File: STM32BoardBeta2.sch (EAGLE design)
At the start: 64 parts, among them IC2 LM2576S, IC3 LM1117IDTX-3.3, IC4 FT232RL, J1 DCJ0202, Q1 8MHz, Q2 32.768KHz, SW1 BOOT, U1 STM32F410R3, X1 MINI-USB-32005-201

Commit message: Cambios en condensador y diodo
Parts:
- C3: device rcl:CPOL-EUE7.5-18 -> rcl:CPOL-EUE5-10.5
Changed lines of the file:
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@@
 <grid distance="0.1" unitdist="inch" unit="inch" style="lines" multiple="1" display="no" altdistance="0.01" altunitdist="inch" altunit="inch"/>
 <layers>
-<layer number="1" name="Top" color="4" fill="1" visible="no" active="no"/>
-<layer number="2" name="Route2" color="1" fill="3" visible="no" active="no"/>
-<layer number="3" name="Route3" color="4" fill="3" visible="no" active="no"/>
-<layer number="4" name="Route4" color="1" fill="4" visible="no" active="no"/>
-<layer number="5" name="Route5" color="4" fill="4" visible="no" active="no"/>
-<layer number="6" name="Route6" color="1" fill="8" visible="no" active="no"/>
-<layer number="7" name="Route7" color="4" fill="8" visible="no" active="no"/>
-<layer number="8" name="Route8" color="1" fill="2" visible="no" active="no"/>
-<layer number="9" name="Route9" color="4" fill="2" visible="no" active="no"/>
-<layer number="10" name="Route10" color="1" fill="7" visible="no" active="no"/>
-<layer number="11" name="Route11" color="4" fill="7" visible="no" active="no"/>
-<layer number="12" name="Route12" color="1" fill="5" visible="no" active="no"/>
-<layer number="13" name="Route13" color="4" fill="5" visible="no" active="no"/>
-<layer number="14" name="Route14" color="1" fill="6" visible="no" active="no"/>
-<layer number="15" name="Route15" color="4" fill="6" visible="no" active="no"/>
-<layer number="16" name="Bottom" color="1" fill="1" visible="no" active="no"/>
-<layer number="17" name="Pads" color="2" fill="1" visible="no" active="no"/>
-<layer number="18" name="Vias" color="2" fill="1" visible="no" active="no"/>
-<layer number="19" name="Unrouted" color="6" fill="1" visible="no" active="no"/>
-<layer number="20" name="Dimension" color="15" fill="1" visible="no" active="no"/>
-<layer number="21" name="tPlace" color="7" fill="1" visible="no" active="no"/>
-<layer number="22" name="bPlace" color="7" fill="1" visible="no" active="no"/>
-<layer number="23" name="tOrigins" color="15" fill="1" visible="no" active="no"/>
-<layer number="24" name="bOrigins" color="15" fill="1" visible="no" active="no"/>
-<layer number="25" name="tNames" color="7" fill="1" visible="no" active="no"/>
-<layer number="26" name="bNames" color="7" fill="1" visible="no" active="no"/>
-<layer number="27" name="tValues" color="7" fill="1" visible="no" active="no"/>
-<layer number="28" name="bValues" color="7" fill="1" visible="no" active="no"/>
+<layer number="1" name="Top" color="4" fill="1" visible="yes" active="no"/>
+<layer number="2" name="Route2" color="1" fill="3" visible="yes" active="no"/>
+<layer number="3" name="Route3" color="4" fill="3" visible="yes" active="no"/>
+<layer number="4" name="Route4" color="1" fill="4" visible="yes" active="no"/>
+<layer number="5" name="Route5" color="4" fill="4" visible="yes" active="no"/>
+<layer number="6" name="Route6" color="1" fill="8" visible="yes" active="no"/>
+<layer number="7" name="Route7" color="4" fill="8" visible="yes" active="no"/>
+<layer number="8" name="Route8" color="1" fill="2" visible="yes" active="no"/>
+<layer number="9" name="Route9" color="4" fill="2" visible="yes" active="no"/>
+<layer number="10" name="Route10" color="1" fill="7" visible="yes" active="no"/>
+<layer number="11" name="Route11" color="4" fill="7" visible="yes" active="no"/>
+<layer number="12" name="Route12" color="1" fill="5" visible="yes" active="no"/>
+<layer number="13" name="Route13" color="4" fill="5" visible="yes" active="no"/>
+<layer number="14" name="Route14" color="1" fill="6" visible="yes" active="no"/>
+<layer number="15" name="Route15" color="4" fill="6" visible="yes" active="no"/>
+<layer number="16" name="Bottom" color="1" fill="1" visible="yes" active="no"/>
+<layer number="17" name="Pads" color="2" fill="1" visible="yes" active="no"/>
+<layer number="18" name="Vias" color="2" fill="1" visible="yes" active="no"/>
+<layer number="19" name="Unrouted" color="6" fill="1" visible="yes" active="no"/>
+<layer number="20" name="Dimension" color="15" fill="1" visible="yes" active="no"/>
+<layer number="21" name="tPlace" color="7" fill="1" visible="yes" active="no"/>
+<layer number="22" name="bPlace" color="7" fill="1" visible="yes" active="no"/>
+<layer number="23" name="tOrigins" color="15" fill="1" visible="yes" active="no"/>
+<layer number="24" name="bOrigins" color="15" fill="1" visible="yes" active="no"/>
+<layer number="25" name="tNames" color="7" fill="1" visible="yes" active="no"/>
+<layer number="26" name="bNames" color="7" fill="1" visible="yes" active="no"/>
+<layer number="27" name="tValues" color="7" fill="1" visible="yes" active="no"/>
+<layer number="28" name="bValues" color="7" fill="1" visible="yes" active="no"/>
 <layer number="29" name="tStop" color="7" fill="3" visible="no" active="no"/>
 <layer number="30" name="bStop" color="7" fill="6" visible="no" active="no"/>
@@
 <layer number="35" name="tGlue" color="7" fill="4" visible="no" active="no"/>
 <layer number="36" name="bGlue" color="7" fill="5" visible="no" active="no"/>
-<layer number="37" name="tTest" color="7" fill="1" visible="no" active="no"/>
-<layer number="38" name="bTest" color="7" fill="1" visible="no" active="no"/>
+<layer number="37" name="tTest" color="7" fill="1" visible="yes" active="no"/>
+<layer number="38" name="bTest" color="7" fill="1" visible="yes" active="no"/>
 <layer number="39" name="tKeepout" color="4" fill="11" visible="no" active="no"/>
 <layer number="40" name="bKeepout" color="1" fill="11" visible="no" active="no"/>
@@
 <layer number="44" name="Drills" color="7" fill="1" visible="no" active="no"/>
 <layer number="45" name="Holes" color="7" fill="1" visible="no" active="no"/>
-<layer number="46" name="Milling" color="3" fill="1" visible="no" active="no"/>
-<layer number="47" name="Measures" color="7" fill="1" visible="no" active="no"/>
-<layer number="48" name="Document" color="7" fill="1" visible="no" active="no"/>
-<layer number="49" name="Reference" color="7" fill="1" visible="no" active="no"/>
-<layer number="50" name="dxf" color="7" fill="1" visible="no" active="no"/>
-<layer number="51" name="tDocu" color="7" fill="1" visible="no" active="no"/>
-<layer number="52" name="bDocu" color="7" fill="1" visible="no" active="no"/>
-<layer number="53" name="tGND_GNDA" color="7" fill="1" visible="no" active="no"/>
-<layer number="54" name="bGND_GNDA" color="7" fill="1" visible="no" active="no"/>
-<layer number="56" name="wert" color="7" fill="1" visible="no" active="no"/>
+<layer number="46" name="Milling" color="3" fill="1" visible="yes" active="no"/>
+<layer number="47" name="Measures" color="7" fill="1" visible="yes" active="no"/>
+<layer number="48" name="Document" color="7" fill="1" visible="yes" active="no"/>
+<layer number="49" name="Reference" color="7" fill="1" visible="yes" active="no"/>
+<layer number="50" name="dxf" color="7" fill="1" visible="yes" active="no"/>
+<layer number="51" name="tDocu" color="7" fill="1" visible="yes" active="no"/>
+<layer number="52" name="bDocu" color="7" fill="1" visible="yes" active="no"/>
+<layer number="53" name="tGND_GNDA" color="7" fill="1" visible="yes" active="no"/>
+<layer number="54" name="bGND_GNDA" color="7" fill="1" visible="yes" active="no"/>
+<layer number="56" name="wert" color="7" fill="1" visible="yes" active="no"/>
 <layer number="90" name="Modules" color="5" fill="1" visible="yes" active="yes"/>
 <layer number="91" name="Nets" color="2" fill="1" visible="yes" active="yes"/>
@@
 <part name="GND3" library="supply1" deviceset="GND" device=""/>
 <part name="D2" library="diode" deviceset="1N4004" device="" value="1N5822"/>
-<part name="C3" library="rcl" deviceset="CPOL-EU" device="E7.5-18" value="1000uF"/>
+<part name="C3" library="rcl" deviceset="CPOL-EU" device="E5-10.5" value="1000uF"/>
 <part name="GND4" library="supply1" deviceset="GND" device=""/>
 <part name="IC3" library="lm1117" deviceset="LM1117IDTX-*" device="" technology="3.3"/>

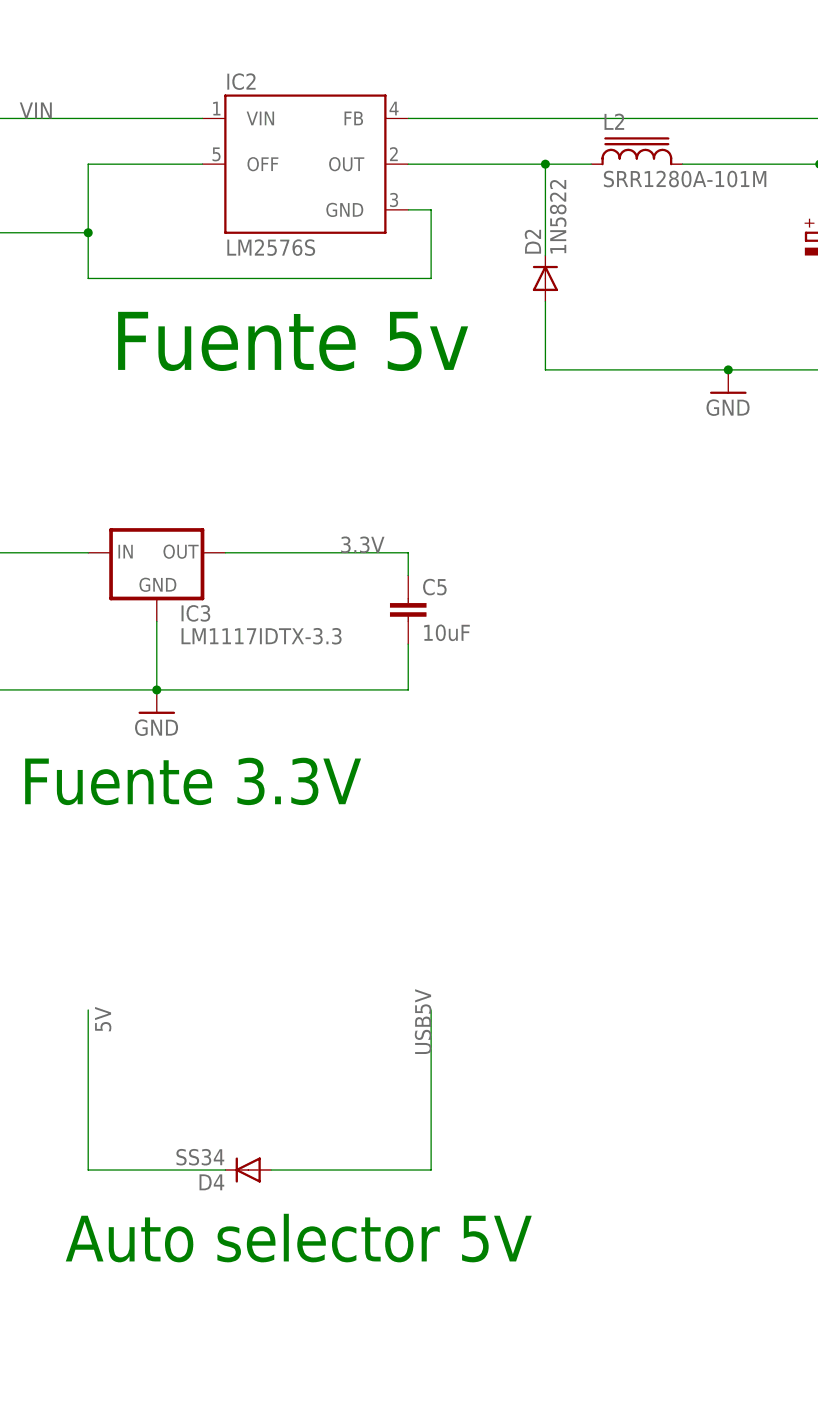
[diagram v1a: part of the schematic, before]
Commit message: Actualización del diodo 1N5822, SS34 y cambio del tamaño del condensador
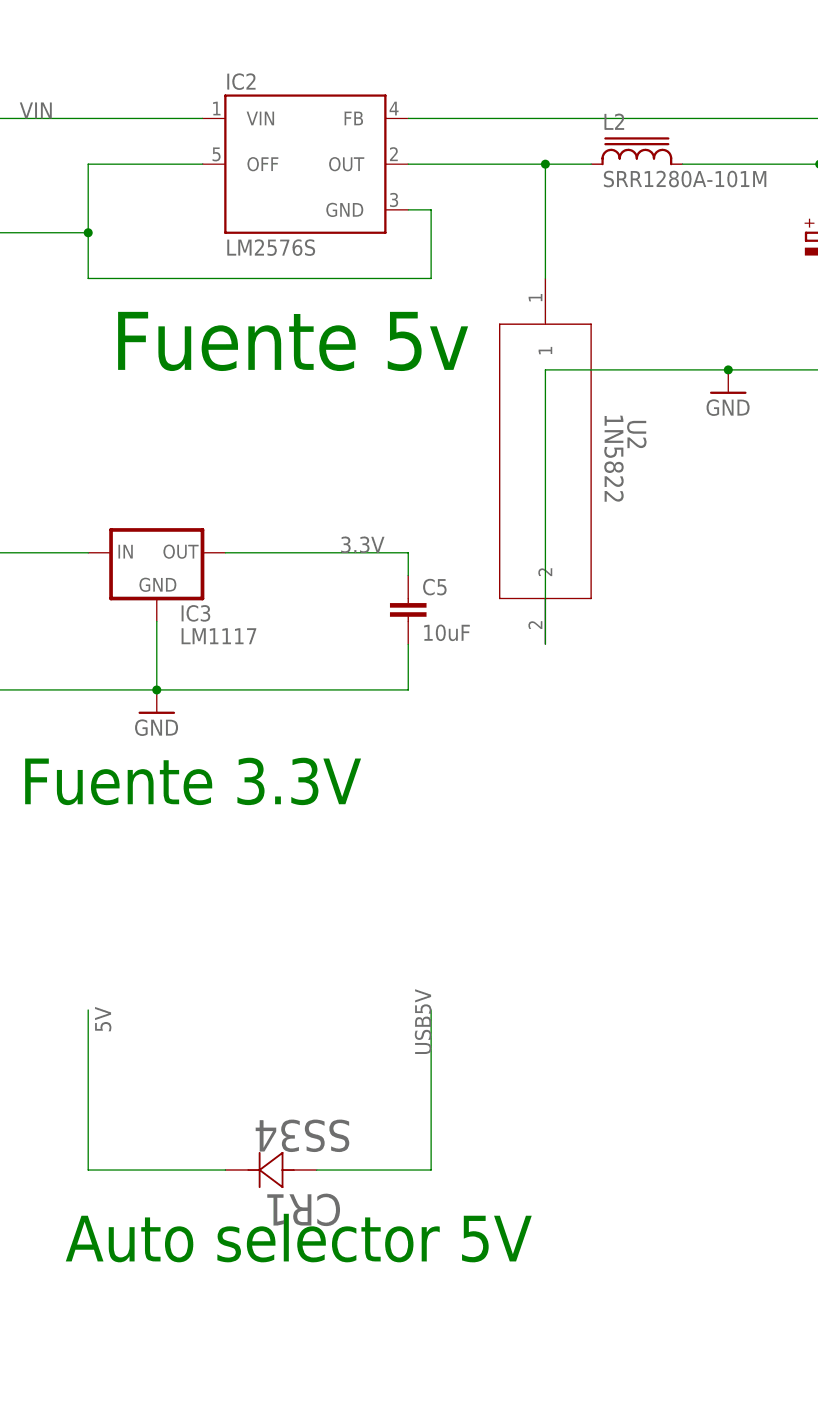
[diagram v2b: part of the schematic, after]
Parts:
- removed D2: 1N5822, diode:1N4004
- removed D4: SS34, diode:DIODE-DO-214AC
- added CR1: SS34, ss34:SS34-E3/57TDIODE_DO214AB-M
- added U2: 1N5822, 1N5822:1N5822RLG
- IC3: value LM1117IDTX-3.3 -> LM1117
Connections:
- net 5V: now also CR1.1; no longer D4.C
- net GND: now also U2.2; no longer D2.A
- net N$4: now also U2.1; no longer D2.C
- net USB5V: now also CR1.2; no longer D4.A
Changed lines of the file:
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@@
 <part name="C2" library="rcl" deviceset="CPOL-EU" device="153CLV-0605" value="100uF"/>
 <part name="GND3" library="supply1" deviceset="GND" device=""/>
-<part name="D2" library="diode" deviceset="1N4004" device="" value="1N5822"/>
 <part name="C3" library="rcl" deviceset="CPOL-EU" device="E5-10.5" value="1000uF"/>
 <part name="GND4" library="supply1" deviceset="GND" device=""/>
-<part name="IC3" library="lm1117" deviceset="LM1117IDTX-*" device="" technology="3.3"/>
+<part name="IC3" library="lm1117" deviceset="LM1117IDTX-*" device="" technology="3.3" value="LM1117"/>
 <part name="C4" library="rcl" deviceset="C-EU" device="C1206K" value="10uF"/>
 <part name="C5" library="rcl" deviceset="C-EU" device="C1206K" value="10uF"/>
@@
 <part name="R1" library="rcl" deviceset="R-EU_" device="M1206" value="0"/>
 <part name="C6" library="rcl" deviceset="C-EU" device="C0805K" value="100n"/>
-<part name="D4" library="diode" deviceset="DIODE-" device="DO-214AC" value="SS34"/>
 <part name="LED1" library="led" deviceset="LED" device="CHIP-LED0805" value="LED_ON"/>
 <part name="R2" library="rcl" deviceset="R-EU_" device="R0805" value="470"/>
@@
 <part name="L2" library="inductor-bourns" deviceset="SRR1280" device="" value="SRR1280A-101M "/>
 <part name="L4" library="resistor" deviceset="R-EU_" device="M0805" value="MI0805K400R"/>
+<part name="CR1" library="ss34" deviceset="SS34-E3/57T" device="DIODE_DO214AB-M" value="SS34"/>
+<part name="U2" library="1N5822" deviceset="1N5822RLG" device="" value="1N5822"/>
 </parts>
 <sheets>
@@
 <instance part="C2" gate="G$1" x="-208.28" y="43.18"/>
 <instance part="GND3" gate="1" x="-208.28" y="30.48"/>
-<instance part="D2" gate="1" x="-139.7" y="30.48" rot="R90"/>
 <instance part="C3" gate="G$1" x="-109.22" y="35.56"/>
 <instance part="GND4" gate="1" x="-119.38" y="17.78"/>
@@
 <instance part="R1" gate="G$1" x="-127" y="149.86"/>
 <instance part="C6" gate="G$1" x="-116.84" y="134.62"/>
-<instance part="D4" gate="G$1" x="-172.72" y="-68.58" rot="R180"/>
 <instance part="LED1" gate="G$1" x="-81.28" y="127"/>
 <instance part="R2" gate="G$1" x="-81.28" y="139.7" rot="R90"/>
@@
 <instance part="L2" gate="G$1" x="-129.54" y="43.18"/>
 <instance part="L4" gate="G$1" x="-17.78" y="88.9"/>
+<instance part="CR1" gate="A" x="-165.1" y="-68.58" rot="R180"/>
+<instance part="U2" gate="A" x="-139.7" y="33.02" rot="R270"/>
 </instances>
 <busses>
@@
 <wire x1="-109.22" y1="20.32" x2="-119.38" y2="20.32" width="0.1524" layer="91"/>
 <wire x1="-119.38" y1="20.32" x2="-139.7" y2="20.32" width="0.1524" layer="91"/>
-<wire x1="-139.7" y1="20.32" x2="-139.7" y2="27.94" width="0.1524" layer="91"/>
-<pinref part="D2" gate="1" pin="A"/>
 <pinref part="GND4" gate="1" pin="GND"/>
 <junction x="-119.38" y="20.32"/>
+<pinref part="U2" gate="A" pin="2"/>
+<wire x1="-139.7" y1="-10.16" x2="-139.7" y2="20.32" width="0.1524" layer="91"/>
 </segment>
 <segment>
@@
 <pinref part="IC2" gate="A" pin="OUT"/>
 <wire x1="-154.94" y1="43.18" x2="-139.7" y2="43.18" width="0.1524" layer="91"/>
-<wire x1="-139.7" y1="43.18" x2="-139.7" y2="33.02" width="0.1524" layer="91"/>
-<pinref part="D2" gate="1" pin="C"/>
-<wire x1="-134.62" y1="43.18" x2="-139.7" y2="43.18" width="0.1524" layer="91"/>
+<pinref part="L2" gate="G$1" pin="1"/>
+<pinref part="U2" gate="A" pin="1"/>
+<wire x1="-139.7" y1="43.18" x2="-134.62" y2="43.18" width="0.1524" layer="91"/>
+<wire x1="-139.7" y1="30.48" x2="-139.7" y2="43.18" width="0.1524" layer="91"/>
 <junction x="-139.7" y="43.18"/>
-<pinref part="L2" gate="G$1" pin="1"/>
 </segment>
 </net>
@@
 </segment>
 <segment>
-<pinref part="D4" gate="G$1" pin="C"/>
-<wire x1="-175.26" y1="-68.58" x2="-190.5" y2="-68.58" width="0.1524" layer="91"/>
 <wire x1="-190.5" y1="-68.58" x2="-190.5" y2="-50.8" width="0.1524" layer="91"/>
 <label x="-187.96" y="-53.34" size="1.778" layer="95" rot="R90"/>
+<pinref part="CR1" gate="A" pin="1"/>
+<wire x1="-175.26" y1="-68.58" x2="-190.5" y2="-68.58" width="0.1524" layer="91"/>
 </segment>
 <segment>
@@
 <segment>
 <wire x1="-152.4" y1="-50.8" x2="-152.4" y2="-68.58" width="0.1524" layer="91"/>
-<wire x1="-152.4" y1="-68.58" x2="-170.18" y2="-68.58" width="0.1524" layer="91"/>
-<pinref part="D4" gate="G$1" pin="A"/>
 <label x="-152.4" y="-55.88" size="1.778" layer="95" rot="R90"/>
-</segment>
-</net>
+<pinref part="CR1" gate="A" pin="2"/>
+<wire x1="-165.1" y1="-68.58" x2="-152.4" y2="-68.58" width="0.1524" layer="91"/>
+</segment>
+</net>

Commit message: Cambio en los condensadores 0201 a 0805
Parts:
- C11, C29: device rcl:C-EUC0201 -> rcl:C-EUC0805K
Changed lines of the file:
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@@
 <part name="U1" library="smr32f410rbt6" deviceset="STM32F410R3" device=""/>
 <part name="R6" library="rcl" deviceset="R-EU_" device="R0402" value="47"/>
-<part name="C11" library="rcl" deviceset="C-EU" device="C0201" value="100n"/>
+<part name="C11" library="rcl" deviceset="C-EU" device="C0805K" value="100n"/>
 <part name="C13" library="rcl" deviceset="C-EU" device="C0603" value="1uf"/>
 <part name="GND10" library="supply1" deviceset="GND" device=""/>
@@
 <part name="GND19" library="supply1" deviceset="GND" device=""/>
 <part name="GND20" library="supply1" deviceset="GND" device=""/>
-<part name="C29" library="rcl" deviceset="C-EU" device="C0201" value="100n"/>
+<part name="C29" library="rcl" deviceset="C-EU" device="C0805K" value="100n"/>
 <part name="R10" library="rcl" deviceset="R-EU_" device="R0805" value="10K"/>
 <part name="R11" library="rcl" deviceset="R-EU_" device="R0805" value="10K"/>
